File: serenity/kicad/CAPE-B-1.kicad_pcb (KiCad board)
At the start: 4 copper layers, 55 x 35 mm, 39 parts

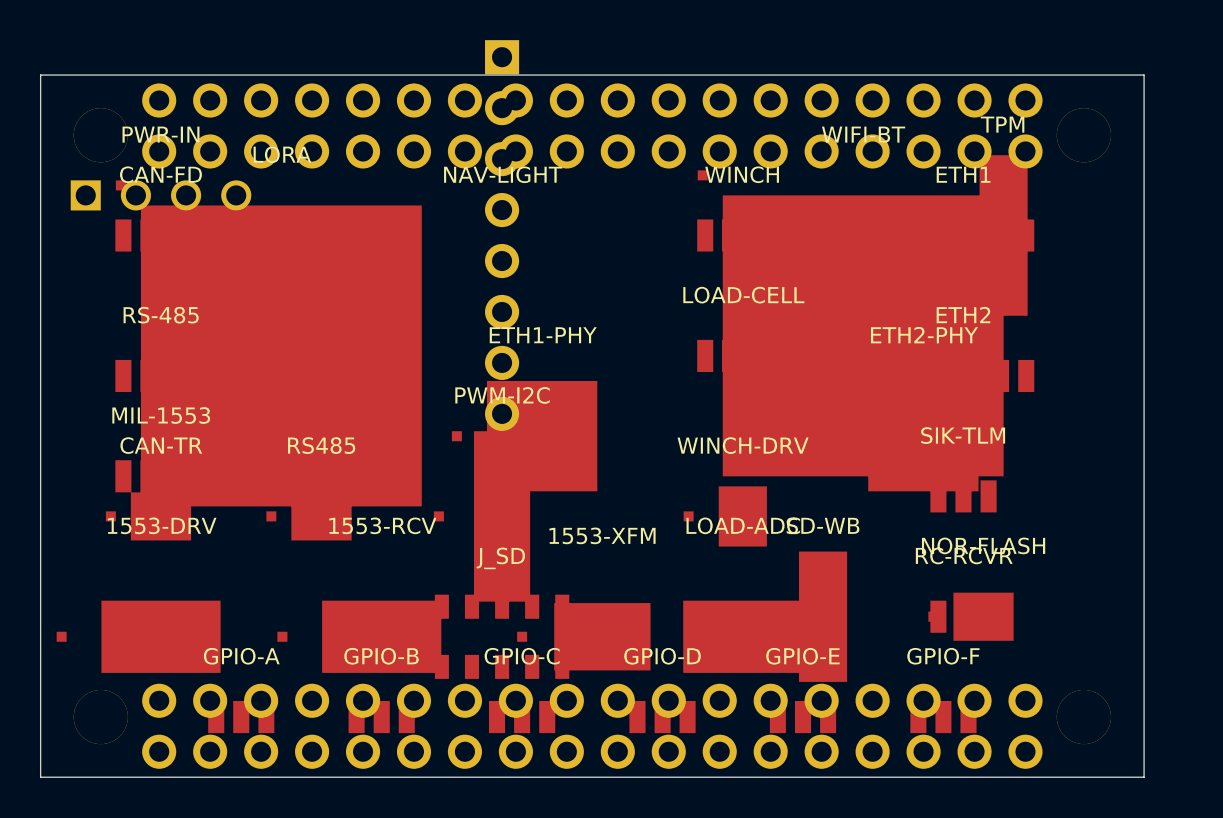
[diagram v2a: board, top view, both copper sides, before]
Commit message: Correct placement: flip RF/storage to B.Cu on CAPE-B-1; revert CAPE-A-1
CAPE-B-1.kicad_pcb:
- Flip existing RFM95W LoRa, WL1837MOD WiFi/BT, ATF16V8BQL CPLD
  write-blocker, W25Q128JV NOR flash, and microSD log slot from F.Cu
  to B.Cu (layer, silk, fab, courtyard, pad layers, justify mirror)
- Update title comment to distinguish F/B component inventory

CAPE-A-1.kicad_pcb:
- Revert erroneously added back-side RF/storage footprints and nets
- Restore original title comment (front-only sensor/comms cape)

https://claude.ai/code/session_01GniMw4QukTVM7JMzyVjH6p
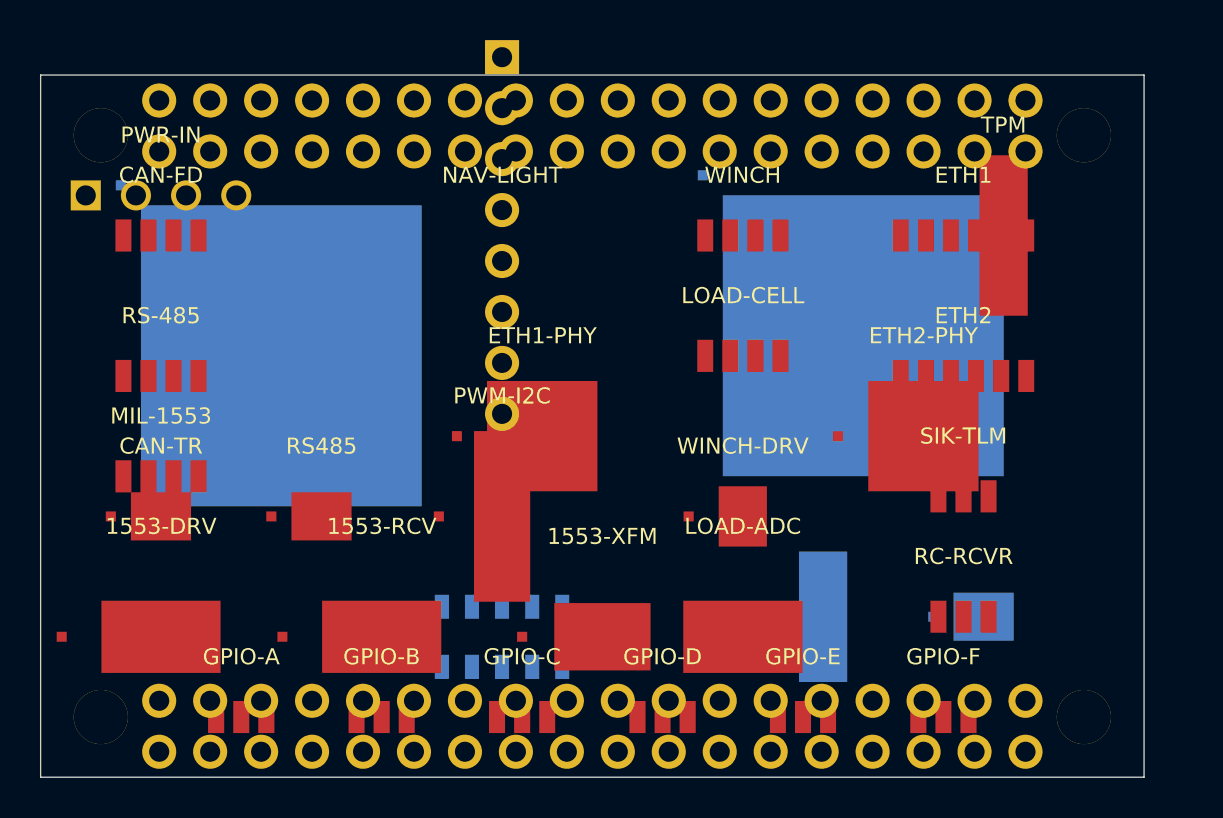
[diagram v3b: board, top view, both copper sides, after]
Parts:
- J_SD, LORA, NOR-FLASH, SD-WB, WIFI-BT: moved to B.Cu
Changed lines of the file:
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@@
     (comment 2 "CC BY 4.0 creativecommons.org/licenses/by/4.0")
     (comment 3 "PocketBeagle 2 Industrial (AM6254) expansion — 55x35mm 4L JLCPCB assembled")
-    (comment 4 "RFM95W LoRa | WL1837MOD WiFi/BT | ATA6561 CAN FD | MAX3485E RS-485 | DS26LV31/32 1553 | DP83825I x2 ETH | SLB9670 TPM2 | ATF16V8BQL CPLD | W25Q128JV NOR | DRV8833 Winch | HX711 Load Cell | PCA9685 PWM | microSD log slot")
+    (comment 4 "F: ATA6561 CAN FD | MAX3485E RS-485 | DS26LV31/32 1553 | DP83825I x2 ETH | SLB9670 TPM2 | DRV8833 Winch | HX711 Load Cell | PCA9685 PWM | B: RFM95W LoRa | WL1837MOD WiFi/BT | ATF16V8BQL CPLD | W25Q128JV NOR | microSD log slot")
     (comment 5 "Hull: Peter Farell CC BY 4.0 | Nozzle: BamJr CC BY 4.0 | Firefly/Serenity fan-work, not officially licensed")
   )
@@
     (pad "35" thru_hole circle (at 21.59 -1.27) (size 1.7 1.7) (drill 1.0) (layers "*.Cu" "*.Mask"))
     (pad "36" thru_hole circle (at 21.59 1.27) (size 1.7 1.7) (drill 1.0) (layers "*.Cu" "*.Mask")))
-  (footprint "RF_Module" (layer "F.Cu") (at 133 101.5) (property "Description" "Hope RFM95W LoRa 868/915MHz SPI module 16x17mm — verify pinout from datasheet")
-    (fp_text reference "LORA" (at 0 -10) (layer "F.SilkS")
-      (effects (font (size 0.8 0.8) (thickness 0.15))))
-    (fp_text value "RFM95W" (at 0 10) (layer "F.Fab")
-      (effects (font (size 0.8 0.8) (thickness 0.15))))
+  (footprint "RF_Module" (layer "B.Cu") (at 133 101.5) (property "Description" "Hope RFM95W LoRa 868/915MHz SPI module 16x17mm — back side, SPI1")
+    (fp_text reference "LORA" (at 0 -10) (layer "B.SilkS")
+      (effects (font (size 0.8 0.8) (thickness 0.15)) (justify mirror)))
+    (fp_text value "RFM95W" (at 0 10) (layer "B.Fab")
+      (effects (font (size 0.8 0.8) (thickness 0.15)) (justify mirror)))
     (fp_poly (pts (xy -8.0 -8.5) (xy 8.0 -8.5) (xy 8.0 8.5) (xy -8.0 8.5))
-     (layer "F.CrtYd") (width 0.05))
-    (pad "1" smd rect (at -8.0 -8.5) (size 0.5 0.5) (layers "F.Cu" "F.Paste" "F.Mask"))
-    (pad "EP" smd rect (at 0 0) (size 14.0 15.0) (layers "F.Cu" "F.Paste" "F.Mask")))
-  (footprint "RF_Module" (layer "F.Cu") (at 162 100.5) (property "Description" "TI WL1837MOD WiFi 802.11bgn BT4.0 SDIO module 16x16mm — verify pinout from datasheet")
-    (fp_text reference "WIFI-BT" (at 0 -10) (layer "F.SilkS")
-      (effects (font (size 0.8 0.8) (thickness 0.15))))
-    (fp_text value "WL1837MOD" (at 0 10) (layer "F.Fab")
-      (effects (font (size 0.8 0.8) (thickness 0.15))))
+     (layer "B.CrtYd") (width 0.05))
+    (pad "1" smd rect (at -8.0 -8.5) (size 0.5 0.5) (layers "B.Cu" "B.Paste" "B.Mask"))
+    (pad "EP" smd rect (at 0 0) (size 14.0 15.0) (layers "B.Cu" "B.Paste" "B.Mask")))
+  (footprint "RF_Module" (layer "B.Cu") (at 162 100.5) (property "Description" "TI WL1837MOD WiFi 802.11bgn BT4.0 SDIO module 16x16mm — back side, SDIO")
+    (fp_text reference "WIFI-BT" (at 0 -10) (layer "B.SilkS")
+      (effects (font (size 0.8 0.8) (thickness 0.15)) (justify mirror)))
+    (fp_text value "WL1837MOD" (at 0 10) (layer "B.Fab")
+      (effects (font (size 0.8 0.8) (thickness 0.15)) (justify mirror)))
     (fp_poly (pts (xy -8.0 -8.0) (xy 8.0 -8.0) (xy 8.0 8.0) (xy -8.0 8.0))
-     (layer "F.CrtYd") (width 0.05))
-    (pad "1" smd rect (at -8.0 -8.0) (size 0.5 0.5) (layers "F.Cu" "F.Paste" "F.Mask"))
-    (pad "EP" smd rect (at 0 0) (size 14.0 14.0) (layers "F.Cu" "F.Paste" "F.Mask")))
+     (layer "B.CrtYd") (width 0.05))
+    (pad "1" smd rect (at -8.0 -8.0) (size 0.5 0.5) (layers "B.Cu" "B.Paste" "B.Mask"))
+    (pad "EP" smd rect (at 0 0) (size 14.0 14.0) (layers "B.Cu" "B.Paste" "B.Mask")))
   (footprint "Package" (layer "F.Cu") (at 127 109.5) (property "Description" "Microchip ATA6561 CAN FD transceiver SOIC-8")
     (fp_text reference "CAN-TR" (at 0 -3.5) (layer "F.SilkS")
@@
     (pad "1" smd rect (at -2.70 0) (size 0.5 0.5) (layers "F.Cu" "F.Paste" "F.Mask"))
     (pad "EP" smd rect (at 0 0) (size 2.40 8.00) (layers "F.Cu" "F.Paste" "F.Mask")))
-  (footprint "Package" (layer "F.Cu") (at 160 114.5) (property "Description" "Microchip ATF16V8BQL GAL CPLD write-blocker for microSD TSSOP-24")
-    (fp_text reference "SD-WB" (at 0 -4.5) (layer "F.SilkS")
-      (effects (font (size 0.8 0.8) (thickness 0.15))))
-    (fp_text value "ATF16V8BQL" (at 0 4.5) (layer "F.Fab")
-      (effects (font (size 0.8 0.8) (thickness 0.15))))
+  (footprint "Package" (layer "B.Cu") (at 160 114.5) (property "Description" "Microchip ATF16V8BQL GAL CPLD write-blocker for microSD TSSOP-24 — back side")
+    (fp_text reference "SD-WB" (at 0 -4.5) (layer "B.SilkS")
+      (effects (font (size 0.8 0.8) (thickness 0.15)) (justify mirror)))
+    (fp_text value "ATF16V8BQL" (at 0 4.5) (layer "B.Fab")
+      (effects (font (size 0.8 0.8) (thickness 0.15)) (justify mirror)))
     (fp_poly (pts (xy -2.70 -4.15) (xy 2.70 -4.15) (xy 2.70 4.15) (xy -2.70 4.15))
-     (layer "F.CrtYd") (width 0.05))
-    (pad "1" smd rect (at -2.70 0) (size 0.5 0.5) (layers "F.Cu" "F.Paste" "F.Mask"))
-    (pad "EP" smd rect (at 0 0) (size 2.40 6.50) (layers "F.Cu" "F.Paste" "F.Mask")))
-  (footprint "Package" (layer "F.Cu") (at 168 114.5) (property "Description" "Winbond W25Q128JV 128Mbit NOR flash SPI SOIC-8")
-    (fp_text reference "NOR-FLASH" (at 0 -3.5) (layer "F.SilkS")
-      (effects (font (size 0.8 0.8) (thickness 0.15))))
-    (fp_text value "W25Q128JV" (at 0 3.5) (layer "F.Fab")
-      (effects (font (size 0.8 0.8) (thickness 0.15))))
+     (layer "B.CrtYd") (width 0.05))
+    (pad "1" smd rect (at -2.70 0) (size 0.5 0.5) (layers "B.Cu" "B.Paste" "B.Mask"))
+    (pad "EP" smd rect (at 0 0) (size 2.40 6.50) (layers "B.Cu" "B.Paste" "B.Mask")))
+  (footprint "Package" (layer "B.Cu") (at 168 114.5) (property "Description" "Winbond W25Q128JV 128Mbit NOR flash SPI SOIC-8 — back side, SPI1")
+    (fp_text reference "NOR-FLASH" (at 0 -3.5) (layer "B.SilkS")
+      (effects (font (size 0.8 0.8) (thickness 0.15)) (justify mirror)))
+    (fp_text value "W25Q128JV" (at 0 3.5) (layer "B.Fab")
+      (effects (font (size 0.8 0.8) (thickness 0.15)) (justify mirror)))
     (fp_poly (pts (xy -2.50 -2.00) (xy 2.50 -2.00) (xy 2.50 2.00) (xy -2.50 2.00))
-     (layer "F.CrtYd") (width 0.05))
-    (pad "1" smd rect (at -2.50 0) (size 0.5 0.5) (layers "F.Cu" "F.Paste" "F.Mask"))
-    (pad "EP" smd rect (at 0 0) (size 3.00 2.40) (layers "F.Cu" "F.Paste" "F.Mask")))
+     (layer "B.CrtYd") (width 0.05))
+    (pad "1" smd rect (at -2.50 0) (size 0.5 0.5) (layers "B.Cu" "B.Paste" "B.Mask"))
+    (pad "EP" smd rect (at 0 0) (size 3.00 2.40) (layers "B.Cu" "B.Paste" "B.Mask")))
   (footprint "Package" (layer "F.Cu") (at 156 109.5) (property "Description" "TI DRV8833 dual H-bridge motor driver HTSSOP-16 — winch motor")
     (fp_text reference "WINCH-DRV" (at 0 -3.5) (layer "F.SilkS")
@@
     (pad "1" smd rect (at -3.15 0) (size 0.5 0.5) (layers "F.Cu" "F.Paste" "F.Mask"))
     (pad "EP" smd rect (at 0 0) (size 2.80 8.50) (layers "F.Cu" "F.Paste" "F.Mask")))
-  (footprint "microSD_Slot" (layer "F.Cu") (at 144 115.5) (property "Description" "microSD push-push slot for write-blocked log storage — Molex 503182-1853 or equiv")
-    (fp_text reference "J_SD" (at 0 -4) (layer "F.SilkS")
-      (effects (font (size 0.8 0.8) (thickness 0.15))))
-    (fp_text value "microSD-Log" (at 0 4) (layer "F.Fab")
-      (effects (font (size 0.8 0.8) (thickness 0.15))))
+  (footprint "microSD_Slot" (layer "B.Cu") (at 144 115.5) (property "Description" "microSD push-push slot for write-blocked log storage — Molex 503182-1853 or equiv — back side")
+    (fp_text reference "J_SD" (at 0 -4) (layer "B.SilkS")
+      (effects (font (size 0.8 0.8) (thickness 0.15)) (justify mirror)))
+    (fp_text value "microSD-Log" (at 0 4) (layer "B.Fab")
+      (effects (font (size 0.8 0.8) (thickness 0.15)) (justify mirror)))
     (fp_poly (pts (xy -7.5 -2.0) (xy 7.5 -2.0) (xy 7.5 2.0) (xy -7.5 2.0))
-     (layer "F.CrtYd") (width 0.05))
-    (pad "1" smd rect (at -3.0 -1.5) (size 0.7 1.2) (layers "F.Cu" "F.Paste" "F.Mask"))
-    (pad "2" smd rect (at -1.5 -1.5) (size 0.7 1.2) (layers "F.Cu" "F.Paste" "F.Mask"))
-    (pad "3" smd rect (at 0.0 -1.5) (size 0.7 1.2) (layers "F.Cu" "F.Paste" "F.Mask"))
-    (pad "4" smd rect (at 1.5 -1.5) (size 0.7 1.2) (layers "F.Cu" "F.Paste" "F.Mask"))
-    (pad "5" smd rect (at 3.0 -1.5) (size 0.7 1.2) (layers "F.Cu" "F.Paste" "F.Mask"))
-    (pad "6" smd rect (at -3.0 1.5) (size 0.7 1.2) (layers "F.Cu" "F.Paste" "F.Mask"))
-    (pad "7" smd rect (at -1.5 1.5) (size 0.7 1.2) (layers "F.Cu" "F.Paste" "F.Mask"))
-    (pad "8" smd rect (at 0.0 1.5) (size 0.7 1.2) (layers "F.Cu" "F.Paste" "F.Mask"))
-    (pad "9" smd rect (at 1.5 1.5) (size 0.7 1.2) (layers "F.Cu" "F.Paste" "F.Mask"))
-    (pad "10" smd rect (at 3.0 1.5) (size 0.7 1.2) (layers "F.Cu" "F.Paste" "F.Mask")))
+     (layer "B.CrtYd") (width 0.05))
+    (pad "1" smd rect (at -3.0 -1.5) (size 0.7 1.2) (layers "B.Cu" "B.Paste" "B.Mask"))
+    (pad "2" smd rect (at -1.5 -1.5) (size 0.7 1.2) (layers "B.Cu" "B.Paste" "B.Mask"))
+    (pad "3" smd rect (at 0.0 -1.5) (size 0.7 1.2) (layers "B.Cu" "B.Paste" "B.Mask"))
+    (pad "4" smd rect (at 1.5 -1.5) (size 0.7 1.2) (layers "B.Cu" "B.Paste" "B.Mask"))
+    (pad "5" smd rect (at 3.0 -1.5) (size 0.7 1.2) (layers "B.Cu" "B.Paste" "B.Mask"))
+    (pad "6" smd rect (at -3.0 1.5) (size 0.7 1.2) (layers "B.Cu" "B.Paste" "B.Mask"))
+    (pad "7" smd rect (at -1.5 1.5) (size 0.7 1.2) (layers "B.Cu" "B.Paste" "B.Mask"))
+    (pad "8" smd rect (at 0.0 1.5) (size 0.7 1.2) (layers "B.Cu" "B.Paste" "B.Mask"))
+    (pad "9" smd rect (at 1.5 1.5) (size 0.7 1.2) (layers "B.Cu" "B.Paste" "B.Mask"))
+    (pad "10" smd rect (at 3.0 1.5) (size 0.7 1.2) (layers "B.Cu" "B.Paste" "B.Mask")))
   (footprint "JST_GH_4P" (layer "F.Cu") (at 127 95.5) (property "Description" "CAN FD external connector — GND CAN_H CAN_L +3V3")
     (fp_text reference "CAN-FD" (at 0 -3) (layer "F.SilkS")

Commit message: Add GPIO expansion headers to CAPE-A-1; add attribution silk to both capes
CAPE-A-1.kicad_pcb:
- Add 6 × JST-GH 3-pin GPIO expansion connectors (GPIO-A through GPIO-F)
  along right edge (X=174) at Y=96/100/104/108/112/116, vertically oriented
  (pads stacked in Y to fit the narrow right-side corridor)
- Add nets GPIO_EXP_A through GPIO_EXP_F (nets 86-91)
- Update title comment to list GPIO expansion headers

CAPE-A-1 + CAPE-B-1:
- Add CC BY 4.0 attribution block as B.SilkS gr_text in the free area
  between the two PocketBeagle 2 socket rows on the back of each cape

https://claude.ai/code/session_01GniMw4QukTVM7JMzyVjH6p
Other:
- board text added: "CC BY 4.0 — Stab-Rabbit-Coding"
- board text added: "Serenity UAV — CN Cape Rev M"
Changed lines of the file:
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@@
     (pad "2" smd rect (at  0.00 0) (size 0.8 1.6) (layers "F.Cu" "F.Paste" "F.Mask"))
     (pad "3" smd rect (at  1.25 0) (size 0.8 1.6) (layers "F.Cu" "F.Paste" "F.Mask")))
+  (gr_text "Serenity UAV — CN Cape Rev M" (at 148.5 103.5) (layer "B.SilkS")
+    (effects (font (size 0.8 0.8) (thickness 0.12)) (justify mirror)))
+  (gr_text "CC BY 4.0 — Stab-Rabbit-Coding" (at 148.5 106.5) (layer "B.SilkS")
+    (effects (font (size 0.8 0.8) (thickness 0.12)) (justify mirror)))
 )
